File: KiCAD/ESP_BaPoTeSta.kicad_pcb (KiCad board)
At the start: 2 copper layers, 31.8 x 44.4 mm, 19 parts, among them P1 Progr, P2 Battery, P3 Power, P4 Upload, P5 Config, U1 MCP1700-330, U2 ESP-12, U3 DS18B20

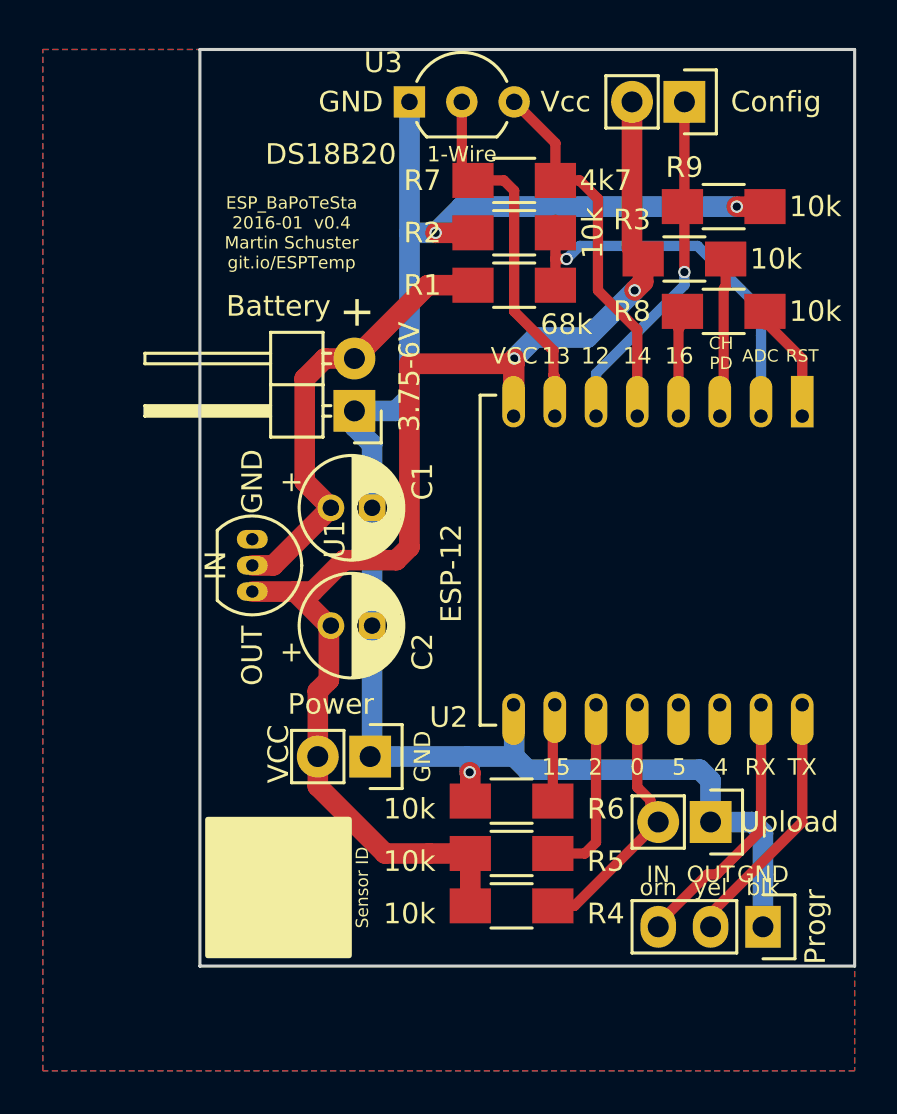
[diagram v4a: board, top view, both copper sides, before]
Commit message: ENH: Improve PCB
Finalize work started in 0493dcc and 57554c2
Add DHT22 (you can now install 2 sensors, DHT22 and DS18B20)
Fix the various bugs (fixes #14, fixes #15, fixes #16)
Avoid ground-fill at DS18B20 GND pin (improves accuracy)
Drop the 2 push-buttons
Board now much smaller (3x5cm)
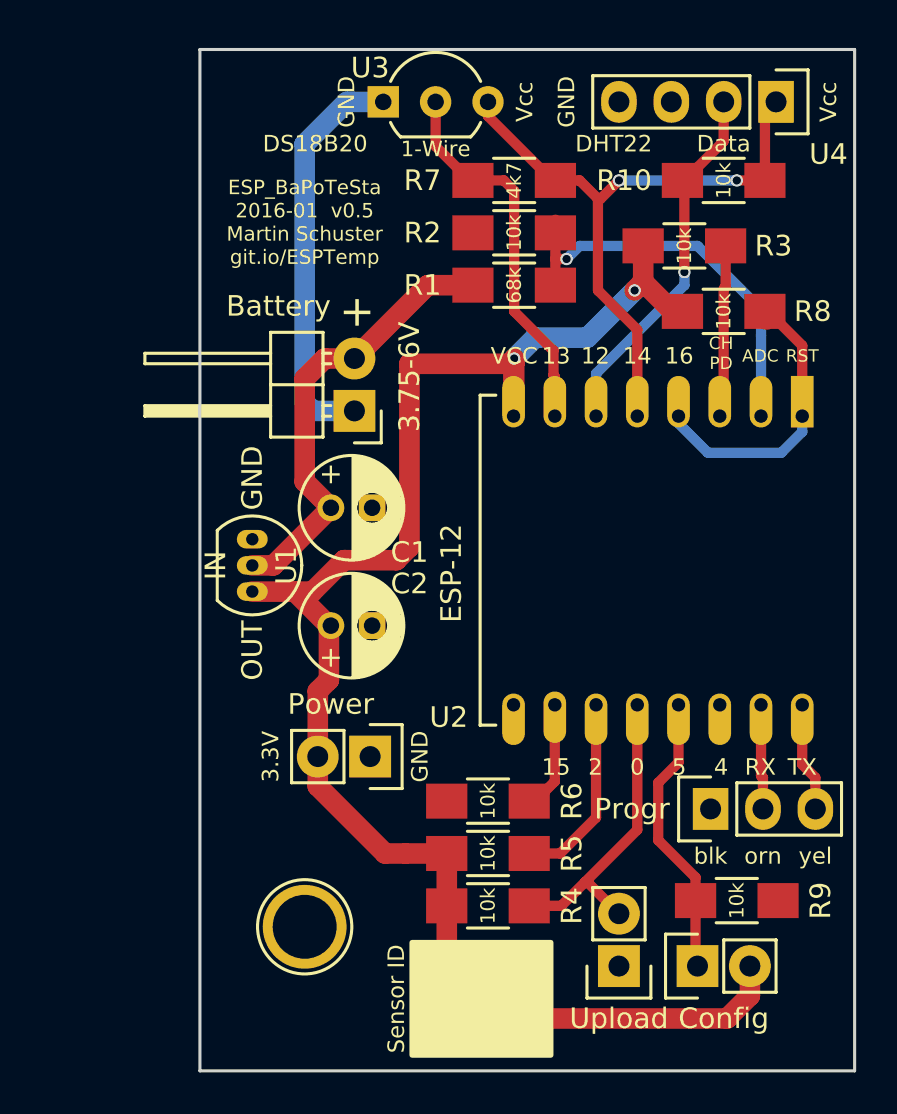
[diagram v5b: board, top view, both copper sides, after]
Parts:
- added R10: 10k, Resistors_SMD:R_1206_HandSoldering, F.Cu at (138.4, 72.4)
- added REF**: 1pin, Connect:1pin, F.Cu at (118.1, 108.6)
- added U4: DHT22, Pin_Headers:Pin_Header_Straight_1x04, F.Cu at (141.0, 68.6)
- moved P5 41.9 mm to (137.2, 110.5), turned to 90 degrees
- moved R9 33.7 mm to (139.1, 107.3)
- moved P4 8.28 mm to (133.3, 110.5), turned to 180 degrees
- moved P1 6.25 mm to (137.8, 102.9), turned to 90 degrees
- moved U3 1.27 mm to (121.9, 68.6)
- moved R4 1.14 mm to (127.0, 107.6)
- moved R5 1.14 mm to (127.0, 105.0)
- moved R6 1.14 mm to (127.0, 102.5)
- moved R3 0.64 mm to (136.5, 75.6)
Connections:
- net /Pwr1W renamed /PwrSens
- R8 pad 1: Net-(R8-Pad1) -> VCC
- U2 pad 13: Net-(U2-Pad13) -> Net-(P5-Pad1)
- U2 pad 15: Net-(P1-Pad3) -> Net-(P1-Pad2)
- U2 pad 16: Net-(P1-Pad2) -> Net-(P1-Pad3)
- U2 pad 4: Net-(R8-Pad1) -> Net-(R8-Pad2)
- U2 pad 6: Net-(P5-Pad1) -> /DHTData
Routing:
- net GND: track 85.1 -> 20.0 mm, vias 3 -> 0
- net /DHTData: track 0.00 -> 17.9 mm, vias 0 -> 1
- net VCC: track 66.2 -> 79.7 mm
- net /PwrSens: track 18.4 -> 31.5 mm, vias 0 -> 2
- net Net-(R8-Pad2): track 5.28 -> 14.2 mm
- net Net-(P1-Pad3): track 13.1 -> 5.31 mm
- net Net-(P1-Pad2): track 12.6 -> 5.09 mm
- net Net-(R8-Pad1): track 4.71 -> 0.00 mm
- net Net-(P5-Pad1): track 17.1 -> 14.0 mm, vias 1 -> 0
- net Net-(P4-Pad2): track 12.6 -> 15.1 mm
- net Net-(R6-Pad2): track 4.80 -> 5.58 mm
- net /1Wire: track 18.0 -> 18.6 mm
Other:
- board size 31.8 x 44.4 mm -> 31.8 x 49.5 mm
- board text added: "3.3V"
- board text added: "Data"
- board text added: "ESP_BaPoTeSta 2016-01 v0.5 Martin Schuster git.io/ESPTemp"
- board text removed: "ESP_BaPoTeSta 2016-01 v0.4 Martin Schuster git.io/ESPTemp"

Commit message: ENH: use small ceramic buffer caps
lower ESR. Still use one additional big electrolytic cap
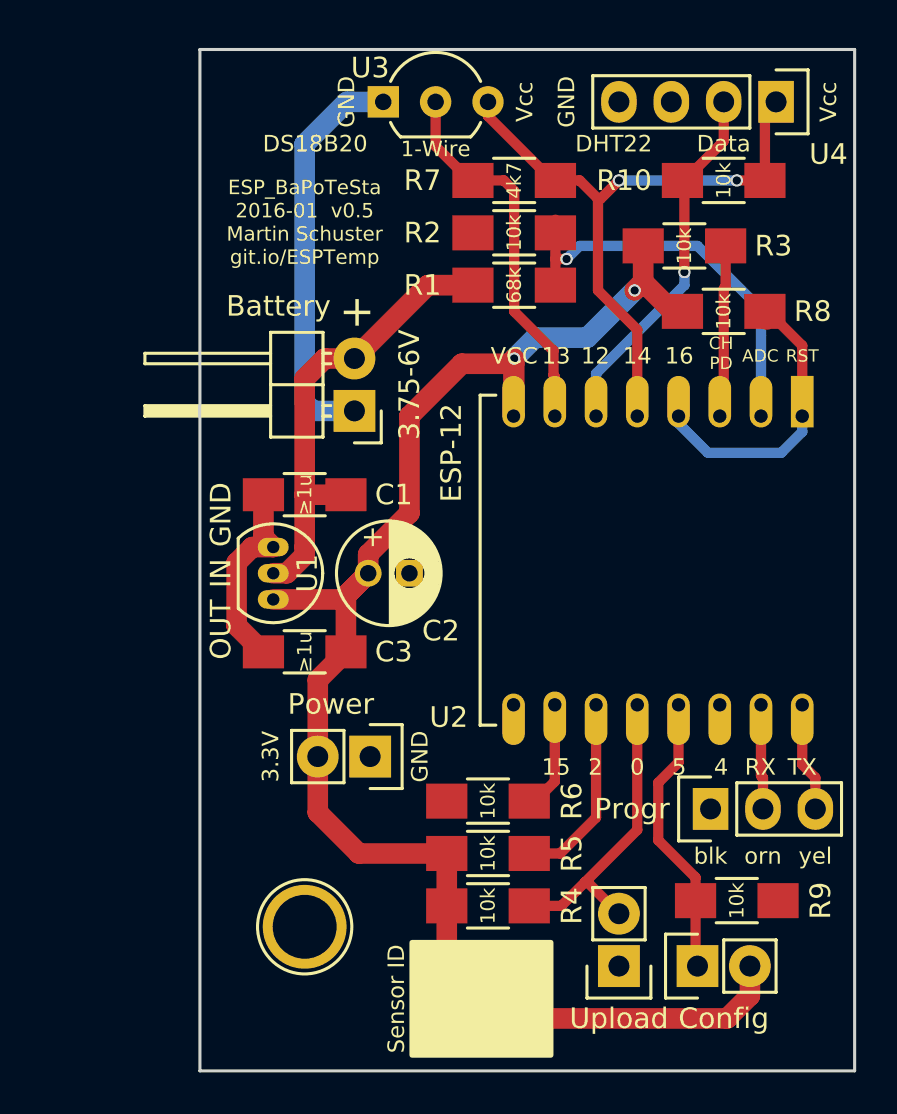
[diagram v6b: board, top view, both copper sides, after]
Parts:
- added C3: ≥1u, Capacitors_SMD:C_1206_HandSoldering, F.Cu at (118.1, 95.2)
- C1: footprint Capacitors_ThroughHole:C_Radial_D5_L11_P2 -> Capacitors_SMD:C_1206_HandSoldering
- C2: value ≥1u -> ≥10u
- moved C2 3.12 mm to (121.2, 91.4)
- moved C1 1.42 mm to (118.1, 87.6), turned to 180 degrees
- moved U1 1.09 mm to (116.6, 90.2)
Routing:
- net GND: track 20.0 -> 29.5 mm
- net VCC: track 79.7 -> 78.8 mm
- net +BATT: track 21.8 -> 22.5 mm

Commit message: ENH: [pcb] grid-align battery header
and minor improvements to tracks
add a via between the ground planes under the ESP
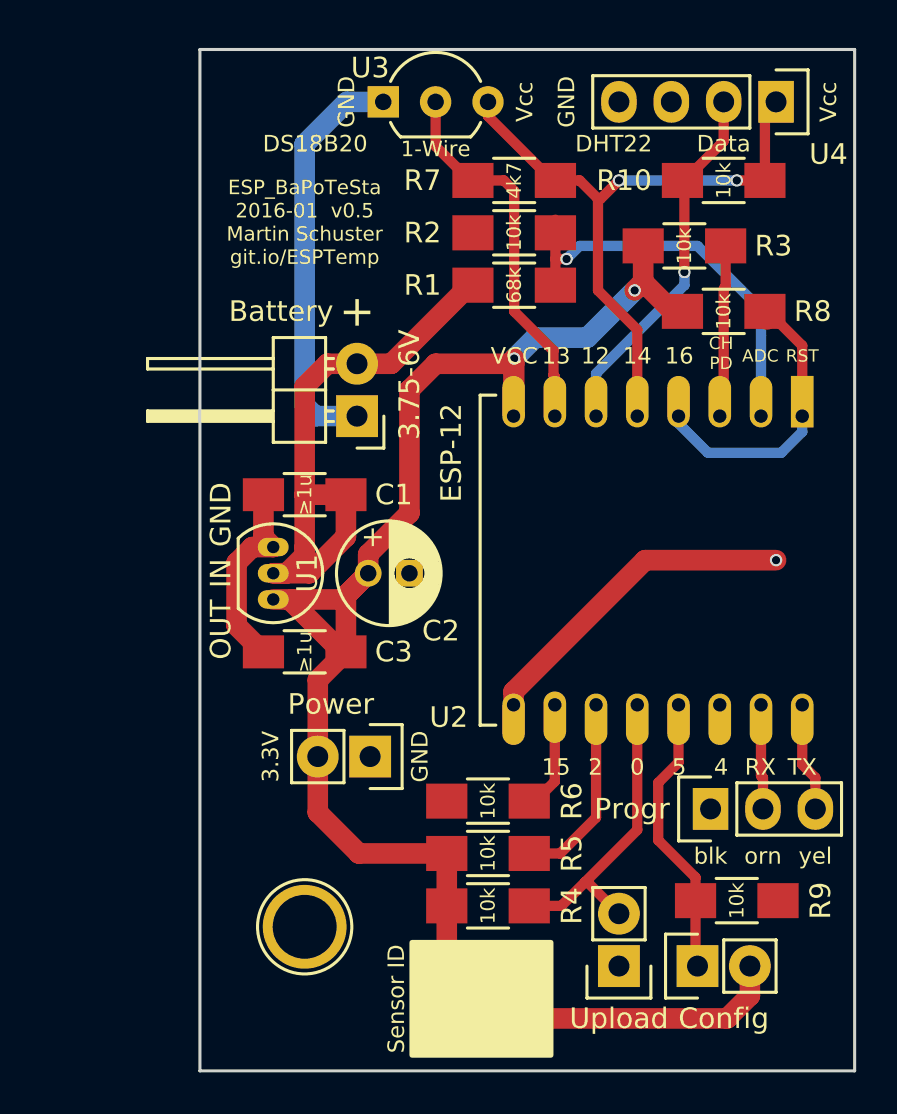
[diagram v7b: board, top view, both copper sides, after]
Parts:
- moved P2 0.28 mm to (120.7, 83.8)
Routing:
- net GND: track 29.5 -> 45.8 mm, vias 0 -> 1
- net +BATT: track 22.5 -> 28.6 mm
- net VCC: track 78.8 -> 83.1 mm
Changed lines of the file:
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@@
     (thickness 1.6)
     (drawings 55)
-    (tracks 144)
+    (tracks 155)
     (zones 0)
     (modules 23)
@@
     (mod_text_size 1 1)
     (mod_text_width 0.15)
-    (pad_size 4.064 4.064)
-    (pad_drill 3.1)
+    (pad_size 1.4 1.4)
+    (pad_drill 1)
     (pad_to_mask_clearance 0.2)
     (aux_axis_origin 113.03 66.04)
@@
   )
   (module Pin_Headers:Pin_Header_Angled_1x02 (layer F.Cu)
-    (at 120.523 83.566 180)
+    (at 120.65 83.82 180)
     (descr "Through hole pin header")
     (tags "pin header")
@@
   (gr_line (start 113.03 115.57) (end 113.03 66.04) (angle 90) (layer Edge.Cuts) (width 0.15))
   (gr_line (start 144.78 66.04) (end 144.78 115.57) (angle 90) (layer Edge.Cuts) (width 0.15))
+  (segment (start 120.11 87.63) (end 120.11 89.66657) (width 1) (layer F.Cu) (net 1))
+  (segment (start 120.11 89.66657) (end 118.33657 91.44) (width 1) (layer F.Cu) (net 1))
+  (segment (start 118.33657 91.44) (end 116.586 91.44) (width 1) (layer F.Cu) (net 1))
+  (segment (start 122.31 81.28) (end 120.65 81.28) (width 1) (layer F.Cu) (net 1))
+  (segment (start 126.27 77.47) (end 126.12 77.47) (width 1) (layer F.Cu) (net 1))
+  (segment (start 126.12 77.47) (end 122.31 81.28) (width 1) (layer F.Cu) (net 1))
+  (segment (start 120.65 81.28) (end 119.21316 81.28) (width 1) (layer F.Cu) (net 1))
+  (segment (start 119.21316 81.28) (end 118.11 82.38316) (width 1) (layer F.Cu) (net 1))
+  (segment (start 118.11 82.38316) (end 118.11 87.63) (width 1) (layer F.Cu) (net 1))
   (segment (start 116.586 91.44) (end 117.242755 91.44) (width 1) (layer F.Cu) (net 1))
   (segment (start 117.242755 91.44) (end 118.11 90.572755) (width 1) (layer F.Cu) (net 1))
   (segment (start 118.11 90.572755) (end 118.11 90.17) (width 1) (layer F.Cu) (net 1))
-  (segment (start 118.11 87.63) (end 118.11 82.00216) (width 1) (layer F.Cu) (net 1))
   (segment (start 120.11 87.63) (end 118.11 87.63) (width 1) (layer F.Cu) (net 1))
   (segment (start 118.11 90.17) (end 118.11 87.63) (width 1) (layer F.Cu) (net 1))
-  (segment (start 120.523 81.026) (end 119.08616 81.026) (width 1) (layer F.Cu) (net 1))
-  (segment (start 119.08616 81.026) (end 118.11 82.00216) (width 1) (layer F.Cu) (net 1))
-  (segment (start 126.27 77.47) (end 124.079 77.47) (width 1) (layer F.Cu) (net 1))
-  (segment (start 124.079 77.47) (end 120.523 81.026) (width 1) (layer F.Cu) (net 1))
+  (segment (start 134.62 90.805) (end 128.24 97.185) (width 1) (layer F.Cu) (net 2))
+  (segment (start 128.24 97.185) (end 128.24 97.82) (width 1) (layer F.Cu) (net 2))
+  (segment (start 140.97 90.805) (end 134.62 90.805) (width 1) (layer F.Cu) (net 2))
+  (via (at 140.97 90.805) (size 0.6) (drill 0.4) (layers F.Cu B.Cu) (net 2))
+  (segment (start 120.65 83.82) (end 118.634 83.82) (width 1) (layer B.Cu) (net 2))
+  (segment (start 118.634 83.82) (end 118.11 83.296) (width 1) (layer B.Cu) (net 2))
+  (segment (start 118.11 83.296) (end 118.11 70.628) (width 1) (layer B.Cu) (net 2))
   (segment (start 114.808 90.932) (end 115.57 90.17) (width 1) (layer F.Cu) (net 2))
   (segment (start 115.57 90.17) (end 116.586 90.17) (width 1) (layer F.Cu) (net 2))
@@
   (segment (start 116.11 87.63) (end 116.11 89.694) (width 1) (layer F.Cu) (net 2))
   (segment (start 116.11 89.694) (end 116.586 90.17) (width 1) (layer F.Cu) (net 2))
-  (segment (start 118.11 70.628) (end 118.11 83.169) (width 1) (layer B.Cu) (net 2))
-  (segment (start 118.11 83.169) (end 118.507 83.566) (width 1) (layer B.Cu) (net 2))
-  (segment (start 118.507 83.566) (end 120.523 83.566) (width 1) (layer B.Cu) (net 2))
   (segment (start 121.92 68.58) (end 120.158 68.58) (width 1) (layer B.Cu) (net 2))
   (segment (start 120.158 68.58) (end 118.11 70.628) (width 1) (layer B.Cu) (net 2))
   (segment (start 128.27 97.85) (end 128.24 97.82) (width 1) (layer B.Cu) (net 2))
-  (segment (start 116.586 92.71) (end 119.92 92.71) (width 1) (layer F.Cu) (net 3))
+  (segment (start 116.586 92.71) (end 117.475 92.71) (width 1) (layer F.Cu) (net 3))
+  (segment (start 117.475 92.71) (end 119.92 92.71) (width 1) (layer F.Cu) (net 3))
+  (segment (start 120.11 95.25) (end 119.91 95.25) (width 1) (layer F.Cu) (net 3))
+  (segment (start 119.91 95.25) (end 117.475 92.815) (width 1) (layer F.Cu) (net 3))
+  (segment (start 117.475 92.815) (end 117.475 92.71) (width 1) (layer F.Cu) (net 3))
+  (segment (start 128.24 81.28) (end 124.46 81.28) (width 1) (layer F.Cu) (net 3))
+  (segment (start 124.46 81.28) (end 123.19 82.55) (width 1) (layer F.Cu) (net 3))
+  (segment (start 123.19 82.55) (end 123.19 88.520762) (width 1) (layer F.Cu) (net 3))
+  (segment (start 123.19 88.520762) (end 121.19 90.520762) (width 1) (layer F.Cu) (net 3))
+  (segment (start 121.19 90.520762) (end 121.19 91.44) (width 1) (layer F.Cu) (net 3))
   (segment (start 119.92 92.71) (end 121.19 91.44) (width 1) (layer F.Cu) (net 3))
   (segment (start 118.745 100.33) (end 118.745 103.03684) (width 1) (layer F.Cu) (net 3))
@@
   (segment (start 118.745 100.33) (end 118.745 96.615) (width 1) (layer F.Cu) (net 3))
   (segment (start 118.745 96.615) (end 120.11 95.25) (width 1) (layer F.Cu) (net 3))
-  (segment (start 120.11 95.25) (end 119.91 95.25) (width 1) (layer F.Cu) (net 3))
   (segment (start 120.11 95.25) (end 120.11 92.52) (width 1) (layer F.Cu) (net 3))
   (segment (start 120.11 92.52) (end 121.19 91.44) (width 1) (layer F.Cu) (net 3))
-  (segment (start 123.19 88.520762) (end 123.19 83.82) (width 1) (layer F.Cu) (net 3))
-  (segment (start 121.19 91.44) (end 121.19 90.520762) (width 1) (layer F.Cu) (net 3))
-  (segment (start 121.19 90.520762) (end 123.19 88.520762) (width 1) (layer F.Cu) (net 3))
-  (segment (start 123.19 83.82) (end 125.73 81.28) (width 1) (layer F.Cu) (net 3))
-  (segment (start 125.73 81.28) (end 128.24 81.28) (width 1) (layer F.Cu) (net 3))
   (segment (start 128.24 81.28) (end 128.24 83.82) (width 1) (layer F.Cu) (net 3))
   (segment (start 136.43 78.74) (end 135.954 78.74) (width 1) (layer F.Cu) (net 3))
